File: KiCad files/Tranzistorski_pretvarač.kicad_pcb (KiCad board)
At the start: 2 copper layers, 94.5 x 79.5 mm, 29 parts, among them J1 Screw_Terminal_01x02, J2 Screw_Terminal_01x02, J3 Conn_01x03_Male, J4 Conn_01x01_Male, J5 Screw_Terminal_01x03, J6 Conn_01x01_Male, J8 Conn_01x01_Male, Q1 IRLZ44N, U1 SG3524, U2 PC817

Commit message: update
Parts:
- added C5: 1000u, Capacitor_THT:CP_Radial_D13.0mm_P5.00mm, F.Cu at (118.4, 68.7)
- moved R4 8.05 mm to (130.4, 65.9)
- moved R5 6.73 mm to (137.0, 65.9)
- moved R7 5.37 mm to (143.5, 65.9)
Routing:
- net /+5V_REF: track 25.4 -> 60.9 mm
- net Net-(J6-Pad1): track 46.1 -> 67.1 mm
- net VDD: track 59.2 -> 39.8 mm
- net Net-(Q1-Pad1): track 32.0 -> 28.3 mm
- net Net-(R5-Pad2): track 38.5 -> 36.4 mm
- net Net-(R6-Pad1): track 51.8 -> 50.5 mm
- net Net-(C4-Pad1): track 42.5 -> 41.7 mm

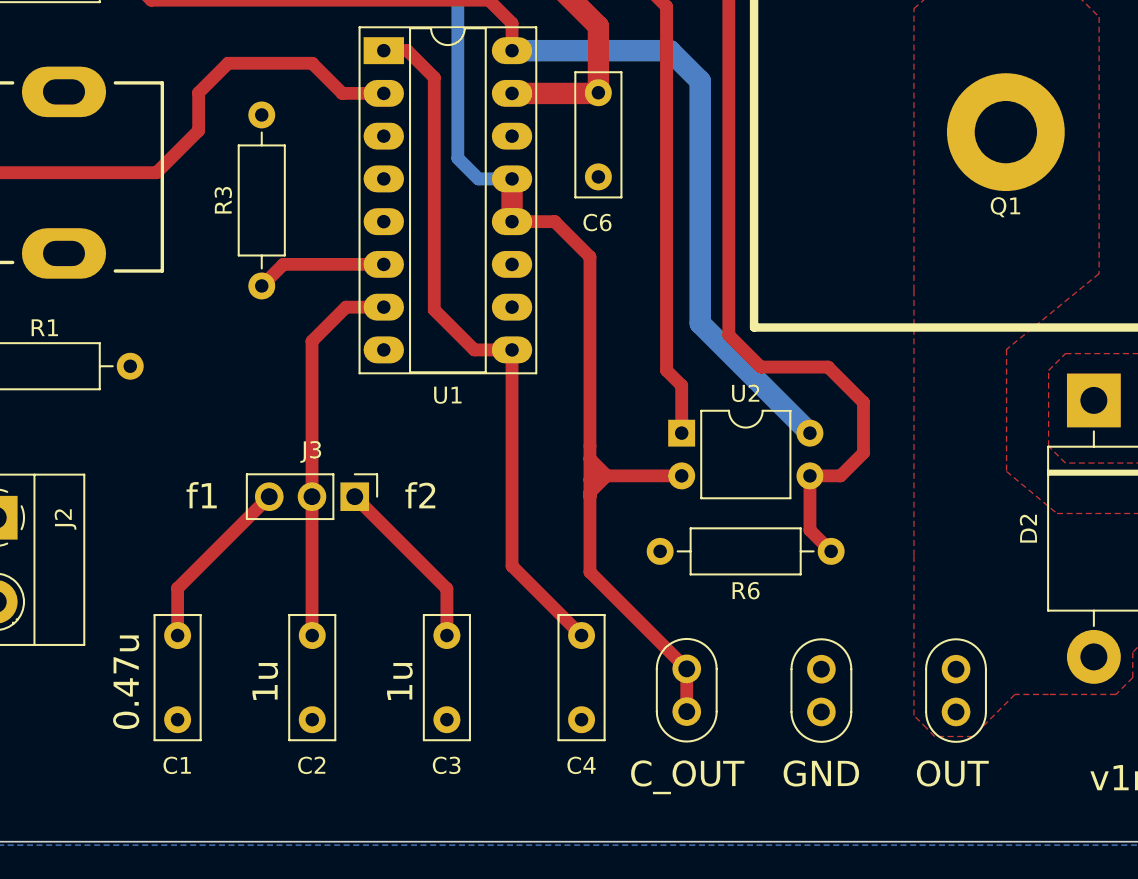
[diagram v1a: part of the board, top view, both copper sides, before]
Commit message: added probe
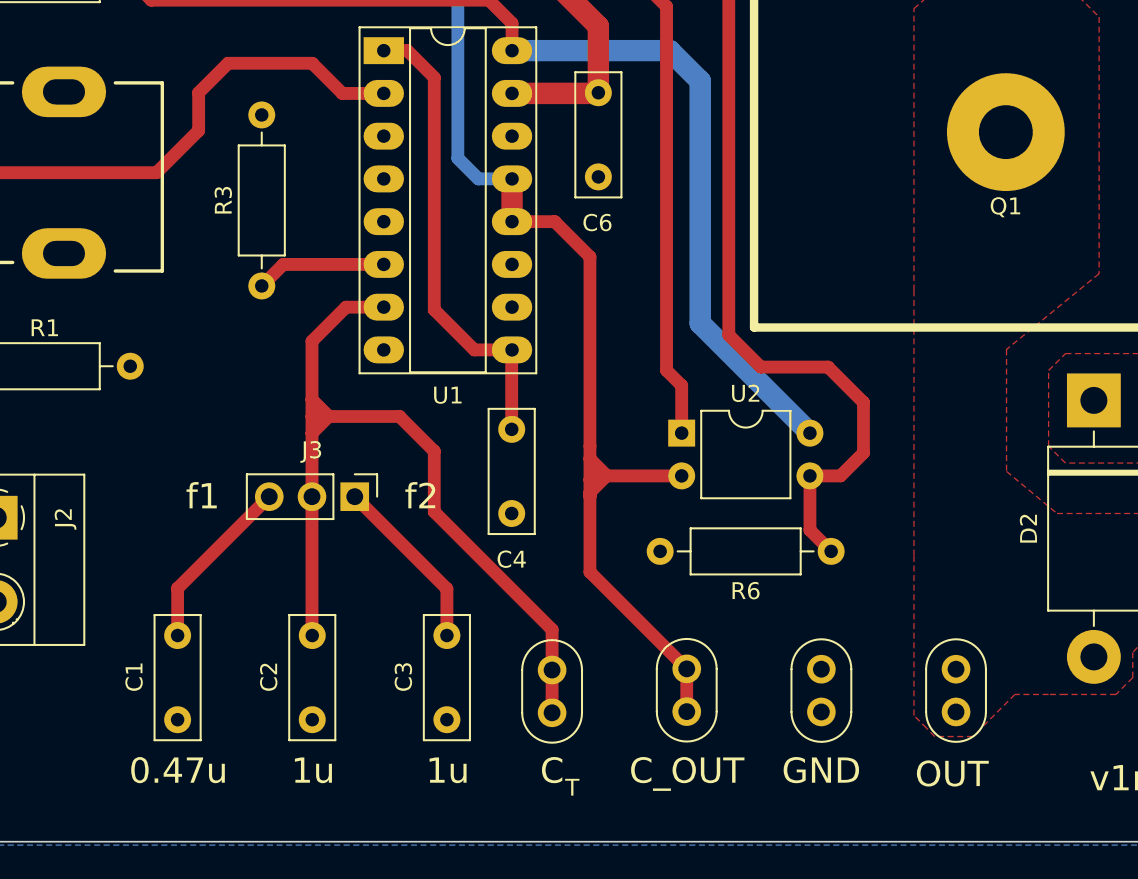
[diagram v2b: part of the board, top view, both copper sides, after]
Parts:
- added J7: Conn_01x01_Male, footprint:oscil, F.Cu at (136.0, 123.8)
- moved C4 12.9 mm to (133.6, 109.5)
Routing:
- net /CT: track 22.6 -> 52.0 mm
- net Net-(C4-Pad1): track 41.7 -> 27.8 mm
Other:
- board text added: "C"
- board text added: "T"

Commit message: banana
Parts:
- J1: value Screw_Terminal_01x02 -> Screw_Terminal_01x01; footprint TerminalBlock_Phoenix:TerminalBlock_Phoenix_MKDS-1,5-2_1x02_P5.00mm_Horizontal -> footprint:DELTRON 4mm banana socket - red
- J2: value Screw_Terminal_01x02 -> Screw_Terminal_01x01; footprint TerminalBlock_Phoenix:TerminalBlock_Phoenix_MKDS-1,5-2_1x02_P5.00mm_Horizontal -> footprint:DELTRON 4mm banana socket - black
- moved J1 4.04 mm to (100.2, 71.2), turned to 0 degrees
- moved J2 3.79 mm to (100.1, 117.2), turned to 0 degrees

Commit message: v2
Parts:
- added J9: Screw_Terminal_01x01, footprint:DELTRON 4mm banana socket - black, F.Cu at (176.5, 139.5)
- J5: value Screw_Terminal_01x03 -> Screw_Terminal_01x01; footprint TerminalBlock_Phoenix:TerminalBlock_Phoenix_MKDS-1,5-3_1x03_P5.00mm_Horizontal -> footprint:DELTRON 4mm banana socket - red
- moved J5 51.1 mm to (176.5, 70.0), turned to 180 degrees
- moved J4 27.2 mm to (143.3, 145.2)
- moved J7 25.8 mm to (121.8, 145.3)
- moved J6 24.4 mm to (132.5, 145.2)
- moved J2 22.0 mm to (101.5, 139.2)
- moved J8 21.6 mm to (154.0, 145.2)
- moved H3 21.1 mm to (92.5, 150.9)
- moved G*** 20.5 mm to (174.5, 149.5)
- moved H1 20.4 mm to (185.2, 150.9)
- moved D2 18.3 mm to (160.5, 124.4)
- moved R6 17.8 mm to (152.1, 134.5)
- moved U2 15.0 mm to (143.2, 124.7)
- moved Q1 14.8 mm to (165.5, 91.7)
- moved C1 12.5 mm to (121.0, 131.9)
- moved C4 12.1 mm to (132.0, 121.5), turned to 180 degrees
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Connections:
- J5 pad 1: GND -> VDD
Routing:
- net /+5V_REF: track 60.9 -> 0.00 mm
- net Net-(R6-Pad1): track 50.5 -> 7.76 mm
- net Net-(J6-Pad1): track 67.1 -> 24.9 mm
- net VDD: track 39.8 -> 0.00 mm
- net Net-(R5-Pad2): track 36.4 -> 0.00 mm
- net Net-(RV1-Pad2): track 30.8 -> 0.00 mm
- net Net-(D2-Pad2): track 0.00 -> 22.1 mm
- net Net-(C4-Pad1): track 27.8 -> 7.89 mm
- net Net-(C3-Pad1): track 10.5 -> 18.0 mm
- net Net-(Q1-Pad1): track 28.3 -> 35.3 mm
- net Net-(R2-Pad2): track 9.32 -> 12.1 mm
- net Net-(R1-Pad1): track 9.32 -> 11.6 mm
- net Net-(C1-Pad1): track 10.5 -> 11.4 mm
- removed copper zone on F.Cu, net Net-(D2-Pad2)
- removed copper zone on F.Cu, net VDD
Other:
- board size 94.5 x 79.5 mm -> 99.9 x 99.9 mm
- board text added: "v2rev1"
- board text removed: "v1rev2"

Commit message: layout
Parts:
- added G***: LOGO, footprint:tvz, F.Cu at (174.0, 140.0)
- moved J2 56.2 mm to (101.0, 83.0)
- moved J5 45.8 mm to (177.0, 115.8)
- moved C1 23.9 mm to (97.0, 133.0)
- moved C2 22.5 mm to (105.5, 133.0)
- moved C3 21.9 mm to (113.0, 133.0)
- moved J3 12.1 mm to (108.0, 125.4)
- moved Q1 11.9 mm to (167.0, 79.9)
- moved G*** 11.5 mm to (174.5, 138.0)
- moved J7 11.1 mm to (121.8, 134.2)
- moved J4 11.0 mm to (143.3, 134.2)
- moved J6 11.0 mm to (132.5, 134.2)
- moved J8 11.0 mm to (154.0, 134.2)
- moved J9 10.5 mm to (177.0, 129.0)
- moved R6 10.4 mm to (146.5, 125.8)
- moved U2 10.4 mm to (137.6, 116.0)
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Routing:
- net Net-(J6-Pad1): track 24.9 -> 77.7 mm
- net /+5V_REF: track 0.00 -> 52.6 mm
- net VDD: track 0.00 -> 39.9 mm
- net Net-(R6-Pad1): track 7.76 -> 47.3 mm
- net Net-(R5-Pad2): track 0.00 -> 39.3 mm
- net Net-(RV1-Pad2): track 0.00 -> 32.2 mm
- net Net-(C4-Pad1): track 7.89 -> 31.6 mm
- net Net-(C3-Pad1): track 18.0 -> 9.67 mm
- net Net-(Q1-Pad1): track 35.3 -> 27.7 mm
- net /CT: track 51.9 -> 59.1 mm
- net GND: track 0.00 -> 2.54 mm
- net Net-(R2-Pad2): track 12.1 -> 9.64 mm
- net Net-(R1-Pad1): track 11.6 -> 10.0 mm
- net Net-(C1-Pad1): track 11.4 -> 10.0 mm
- net Net-(D2-Pad2): track 22.1 -> 21.5 mm
- added copper zone on F.Cu, net Net-(D2-Pad2)
- added copper zone on F.Cu, net VDD
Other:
- board size 99.9 x 99.9 mm -> 99.9 x 92.6 mm
- board text removed: "VDD"
- board text removed: "f1"
- board text removed: "f2"

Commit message: test
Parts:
- removed the G*** at (174.0, 140.0)
- removed R5: 2k, Resistor_THT:R_Axial_DIN0207_L6.3mm_D2.5mm_P10.16mm_Horizontal
- removed U2: PC817, Package_DIP:DIP-4_W7.62mm
- R4: value 10k -> 2k2
- moved R6 12.3 mm to (134.8, 121.9), turned to 0 degrees
- moved R4 5.10 mm to (137.0, 71.4)
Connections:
- R6 pad 1: Net-(R6-Pad1) -> Net-(J6-Pad1)
- R7 pad 2: Net-(R6-Pad1) -> Net-(J6-Pad1)
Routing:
- net Net-(R6-Pad1): track 47.3 -> 0.00 mm
- net Net-(R5-Pad2): track 39.3 -> 0.00 mm
- net /+5V_REF: track 52.6 -> 23.9 mm
- net Net-(J6-Pad1): track 77.7 -> 80.8 mm

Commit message: v3
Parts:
- moved J2 51.8 mm to (101.0, 134.8)
- moved J5 46.1 mm to (176.5, 69.7)
- moved R7 38.0 mm to (139.6, 109.1), turned to 90 degrees
- moved D2 28.7 mm to (181.2, 94.8)
- moved C3 28.1 mm to (140.2, 125.7)
- moved C2 25.8 mm to (130.2, 125.7)
- moved J3 25.8 mm to (132.7, 118.1)
- moved C1 24.3 mm to (120.2, 125.7)
- moved R6 23.0 mm to (133.8, 98.9), turned to -90 degrees
- moved Q1 16.1 mm to (161.5, 95.1)
- moved R3 15.0 mm to (113.4, 96.3), turned to -90 degrees
- moved R4 14.7 mm to (139.6, 85.9)
- moved C4 13.8 mm to (126.9, 108.5)
- moved U1 13.8 mm to (120.9, 83.5)
- moved C6 13.8 mm to (133.8, 86.0)
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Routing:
- net Net-(D2-Pad2): track 21.5 -> 44.0 mm
- net Net-(J6-Pad1): track 80.8 -> 73.5 mm
- net Net-(Q1-Pad1): track 27.7 -> 34.5 mm
- net Net-(RV1-Pad2): track 32.2 -> 36.1 mm
- net VDD: track 39.9 -> 36.3 mm
- net Net-(R2-Pad2): track 9.64 -> 12.8 mm
- net Net-(R1-Pad1): track 10.0 -> 12.8 mm
- net /+5V_REF: track 23.9 -> 26.5 mm
- net GND: track 2.54 -> 0.00 mm
- net Net-(C3-Pad1): track 9.67 -> 10.7 mm
- net Net-(C1-Pad1): track 10.0 -> 10.7 mm
- added copper zone on B.Cu, net Net-(D2-Pad2)
- removed copper zone on F.Cu, net Net-(D2-Pad2)
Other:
- board text added: "COL"
- board text added: "CT"
- board text added: "VDD"
- board text removed: "C"
- board text removed: "C_OUT"
- board text removed: "T"
